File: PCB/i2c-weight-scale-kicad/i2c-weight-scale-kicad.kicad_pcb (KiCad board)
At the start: 2 copper layers, 1 part, among them P1 4_STRAIN_GAUGES

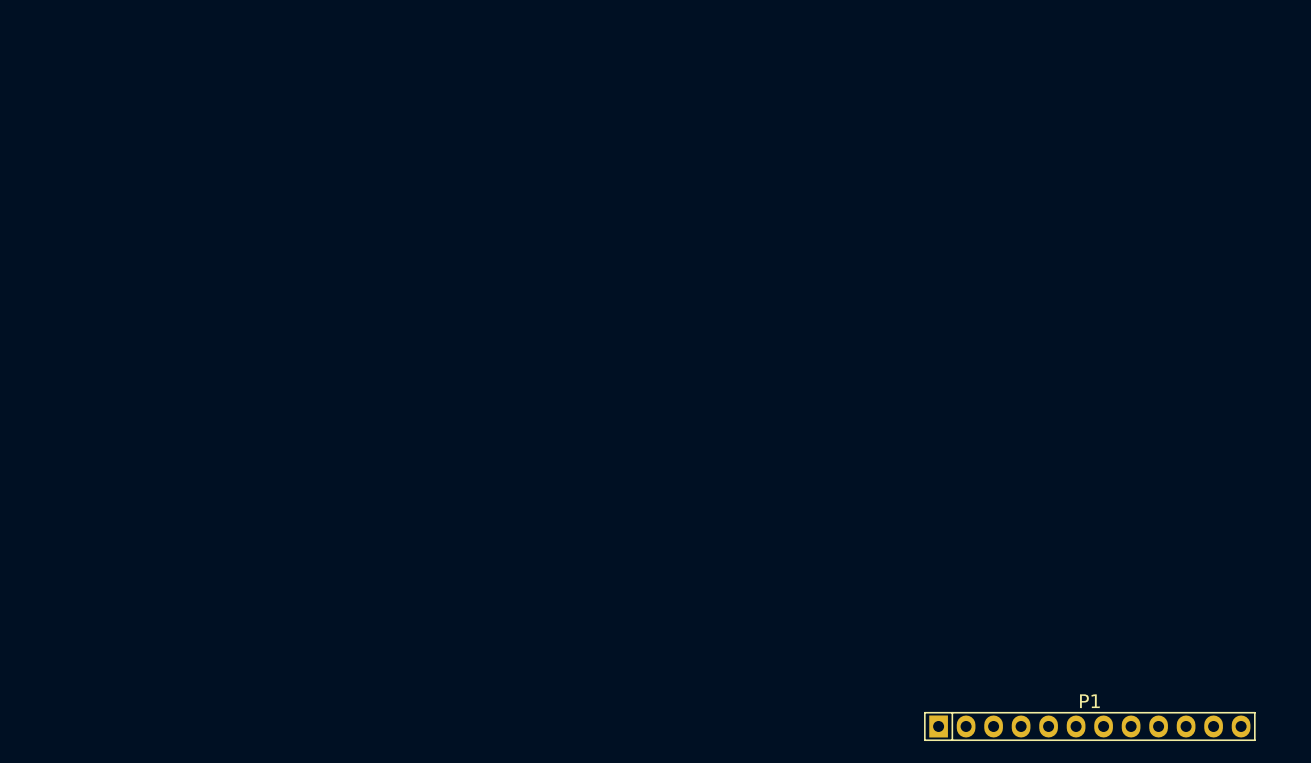
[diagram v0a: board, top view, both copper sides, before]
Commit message: Add all footprints and draw PCB edge cuts
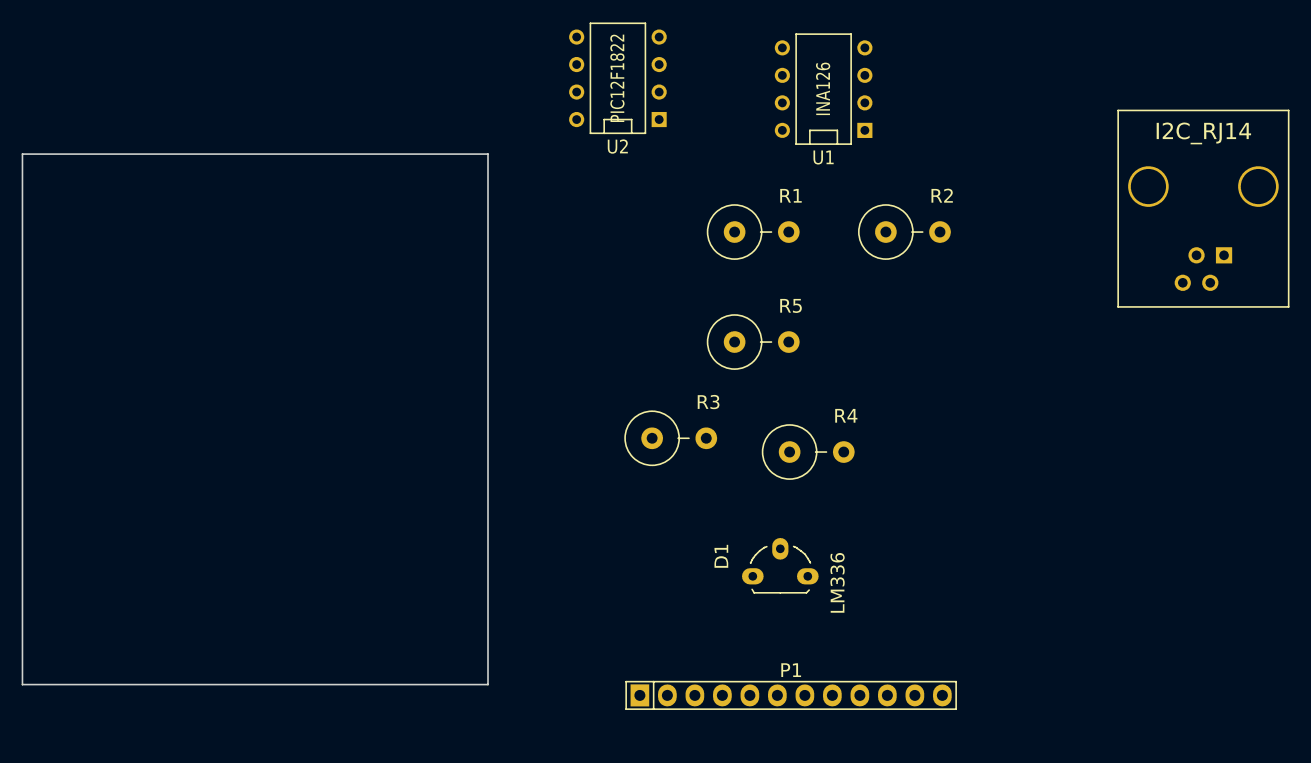
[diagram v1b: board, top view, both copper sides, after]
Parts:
- added D1: LM336, Housings_TO-92:TO-92-Free-molded-wide-oval, F.Cu at (120.0, 89.0)
- added J1: I2C_RJ14, simlun:RJ14_6P4C_right_angle_Molex_95009-7641, F.Cu at (154.0, 53.0)
- added R1: 1K5, Resistors_ThroughHole:Resistor_Vertical_RM5mm, F.Cu at (118.3, 57.2)
- added R2: 1K, Resistors_ThroughHole:Resistor_Vertical_RM5mm, F.Cu at (132.2, 57.2)
- added R3: 82, Resistors_ThroughHole:Resistor_Vertical_RM5mm, F.Cu at (110.7, 76.2)
- added R4: 1K, Resistors_ThroughHole:Resistor_Vertical_RM5mm, F.Cu at (123.4, 77.5)
- added R5: 10K, Resistors_ThroughHole:Resistor_Vertical_RM5mm, F.Cu at (118.3, 67.4)
- added U1: INA126, Sockets_DIP:DIP-8__300, F.Cu at (124.0, 44.0)
- added U2: PIC12F1822, Sockets_DIP:DIP-8__300, F.Cu at (105.0, 43.0)
- moved P1 27.7 mm to (121.0, 100.0)
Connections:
- P1 pad 10: Net-(P1-Pad10) -> Net-(P1-Pad1)
- P1 pad 6: Net-(P1-Pad6) -> Net-(P1-Pad3)
- P1 pad 7: Net-(P1-Pad7) -> Net-(P1-Pad4)
- P1 pad 8: Net-(P1-Pad8) -> GND
- P1 pad 9: Net-(P1-Pad9) -> Net-(P1-Pad12)
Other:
- board outline added: 43 x 49 mm
- rule pad_to_mask_clearance: 0 -> 0.2

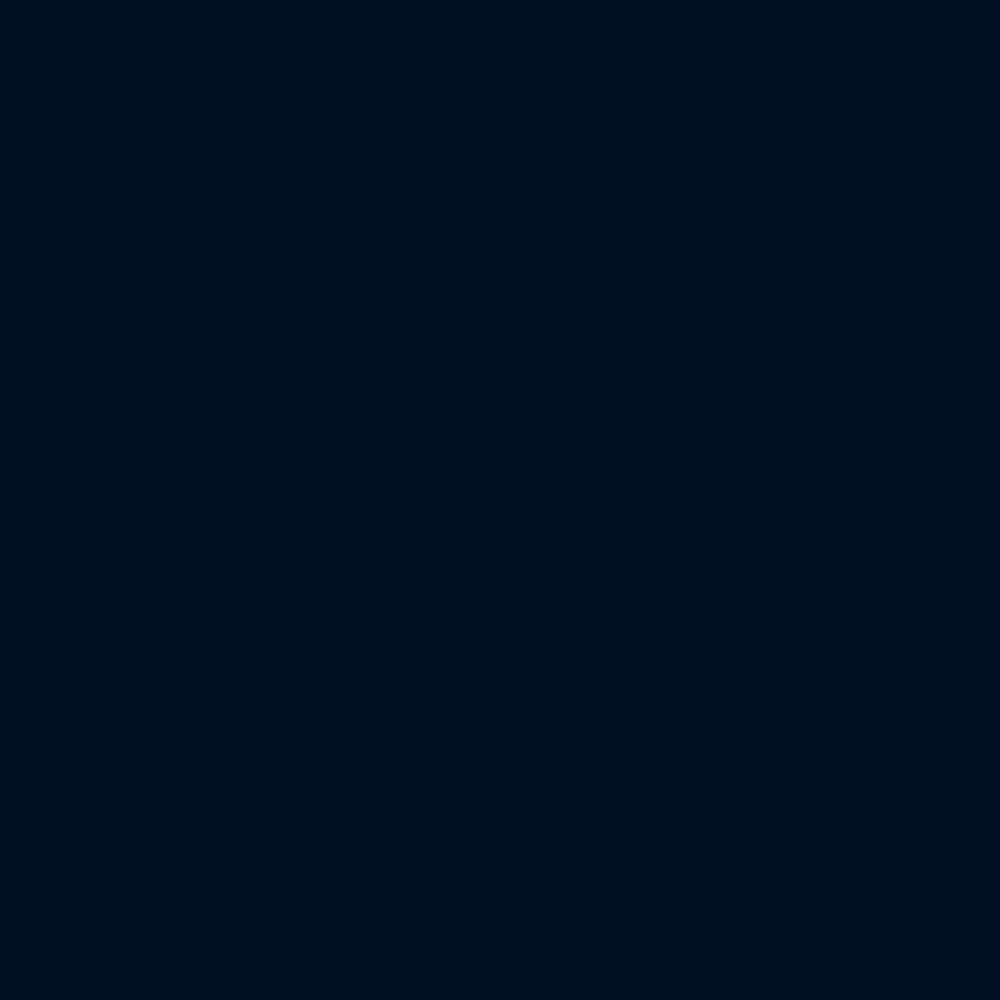
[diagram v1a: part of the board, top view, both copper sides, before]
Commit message: Add mounting holes
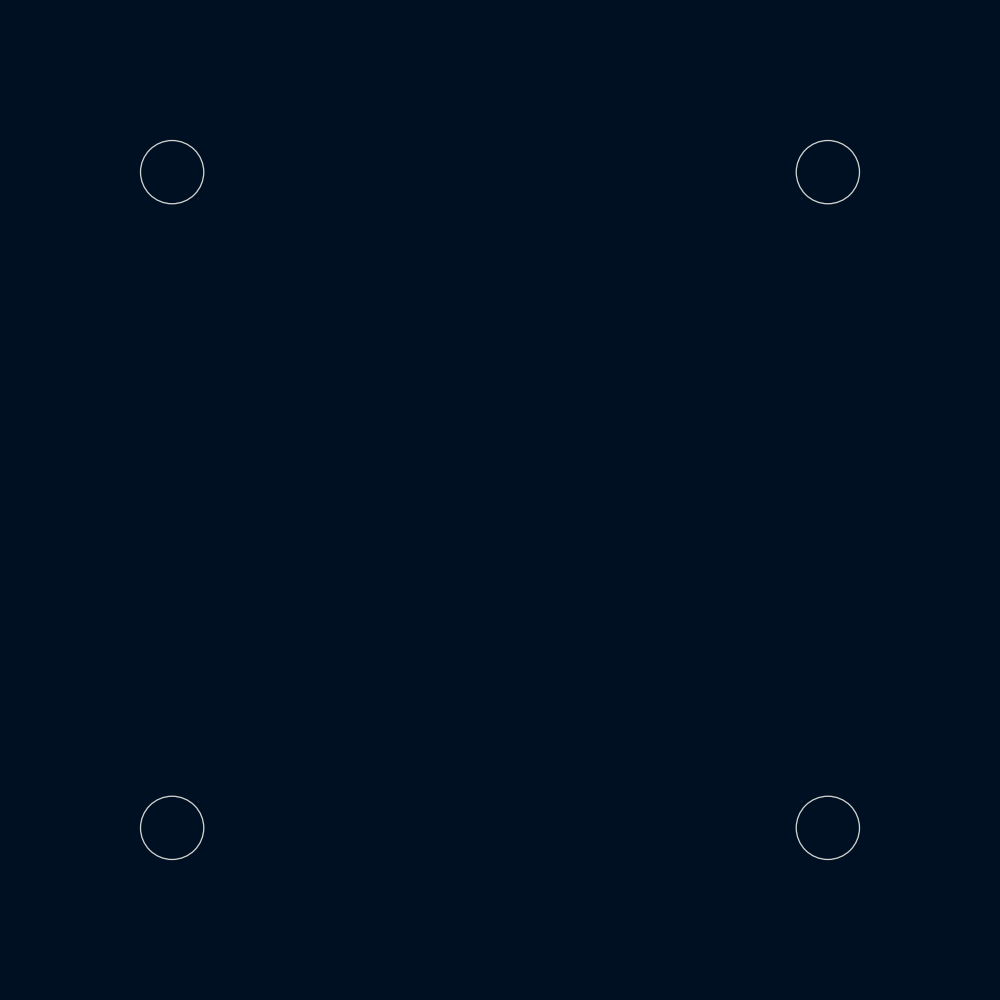
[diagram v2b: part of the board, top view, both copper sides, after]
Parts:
- added MH: MountingHole_2-7mm_RevA_Date21Jun2010, Mounting_Holes:MountingHole_2-7mm, F.Cu at (57.5, 63.6)
- added MH: MountingHole_2-7mm_RevA_Date21Jun2010, Mounting_Holes:MountingHole_2-7mm, F.Cu at (57.5, 91.6)
- added MH: MountingHole_2-7mm_RevA_Date21Jun2010, Mounting_Holes:MountingHole_2-7mm, F.Cu at (85.5, 63.6)
- added MH: MountingHole_2-7mm_RevA_Date21Jun2010, Mounting_Holes:MountingHole_2-7mm, F.Cu at (85.5, 91.6)
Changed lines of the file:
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@@
     (tracks 0)
     (zones 0)
-    (modules 10)
+    (modules 14)
     (nets 20)
   )
@@
       (net 6 VDD))
   )
+  (module Mounting_Holes:MountingHole_2-7mm (layer F.Cu)
+    (at 57.5 63.56)
+    (descr "Mounting hole, Befestigungsbohrung, 2,7mm, No Annular, Kein Restring,")
+    (tags "Mounting hole, Befestigungsbohrung, 2,7mm, No Annular, Kein Restring,")
+    (fp_text reference MH (at 0 -4.0005) (layer F.SilkS) hide
+      (effects (font (thickness 0.3048)))
+    )
+    (fp_text value MountingHole_2-7mm_RevA_Date21Jun2010 (at 0.09906 3.59918) (layer F.SilkS) hide
+      (effects (font (thickness 0.3048)))
+    )
+    (fp_circle (center 0 0) (end 2.70002 0) (layer Cmts.User) (width 0.381))
+    (pad 1 thru_hole circle (at 0 0) (size 2.70002 2.70002) (drill 2.70002) (layers))
+  )
+  (module Mounting_Holes:MountingHole_2-7mm (layer F.Cu)
+    (at 57.5 91.56)
+    (descr "Mounting hole, Befestigungsbohrung, 2,7mm, No Annular, Kein Restring,")
+    (tags "Mounting hole, Befestigungsbohrung, 2,7mm, No Annular, Kein Restring,")
+    (fp_text reference MH (at 0 -4.0005) (layer F.SilkS) hide
+      (effects (font (thickness 0.3048)))
+    )
+    (fp_text value MountingHole_2-7mm_RevA_Date21Jun2010 (at 0.09906 3.59918) (layer F.SilkS) hide
+      (effects (font (thickness 0.3048)))
+    )
+    (fp_circle (center 0 0) (end 2.70002 0) (layer Cmts.User) (width 0.381))
+    (pad 1 thru_hole circle (at 0 0) (size 2.70002 2.70002) (drill 2.70002) (layers))
+  )
+  (module Mounting_Holes:MountingHole_2-7mm (layer F.Cu)
+    (at 85.5 63.56)
+    (descr "Mounting hole, Befestigungsbohrung, 2,7mm, No Annular, Kein Restring,")
+    (tags "Mounting hole, Befestigungsbohrung, 2,7mm, No Annular, Kein Restring,")
+    (fp_text reference MH (at 0 -4.0005) (layer F.SilkS) hide
+      (effects (font (thickness 0.3048)))
+    )
+    (fp_text value MountingHole_2-7mm_RevA_Date21Jun2010 (at 0.09906 3.59918) (layer F.SilkS) hide
+      (effects (font (thickness 0.3048)))
+    )
+    (fp_circle (center 0 0) (end 2.70002 0) (layer Cmts.User) (width 0.381))
+    (pad 1 thru_hole circle (at 0 0) (size 2.70002 2.70002) (drill 2.70002) (layers))
+  )
+  (module Mounting_Holes:MountingHole_2-7mm (layer F.Cu)
+    (at 85.5 91.56)
+    (descr "Mounting hole, Befestigungsbohrung, 2,7mm, No Annular, Kein Restring,")
+    (tags "Mounting hole, Befestigungsbohrung, 2,7mm, No Annular, Kein Restring,")
+    (fp_text reference MH (at 0 -4.0005) (layer F.SilkS) hide
+      (effects (font (thickness 0.3048)))
+    )
+    (fp_text value MountingHole_2-7mm_RevA_Date21Jun2010 (at 0.09906 3.59918) (layer F.SilkS) hide
+      (effects (font (thickness 0.3048)))
+    )
+    (fp_circle (center 0 0) (end 2.70002 0) (layer Cmts.User) (width 0.381))
+    (pad 1 thru_hole circle (at 0 0) (size 2.70002 2.70002) (drill 2.70002) (layers))
+  )
   (gr_line (start 50 99) (end 50 50) (angle 90) (layer Edge.Cuts) (width 0.15))
